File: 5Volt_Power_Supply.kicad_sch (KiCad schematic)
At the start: 12 parts, among them J1 Screw_Terminal_01x02, J2 Screw_Terminal_01x02, U1 L7805

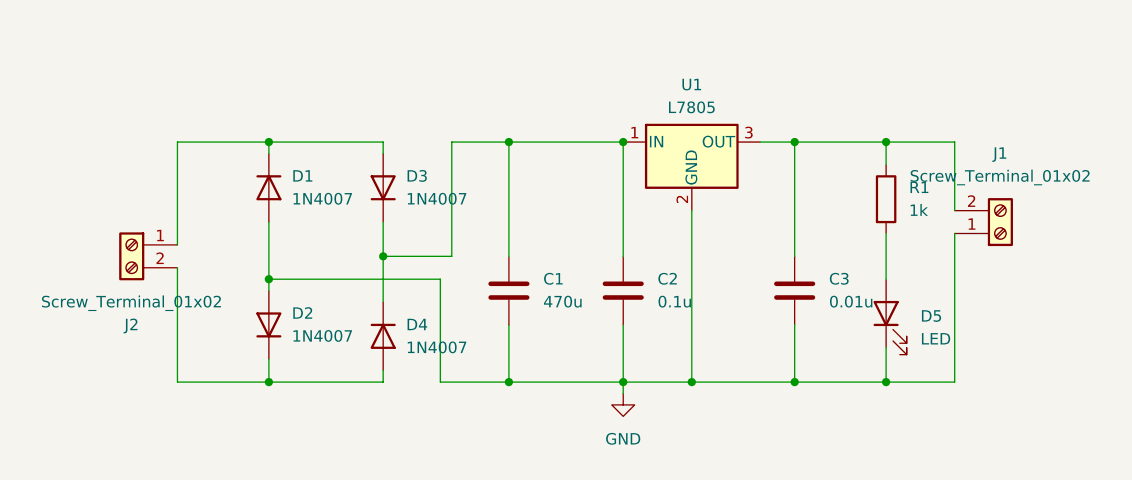
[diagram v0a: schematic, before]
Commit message: schematic pcb views
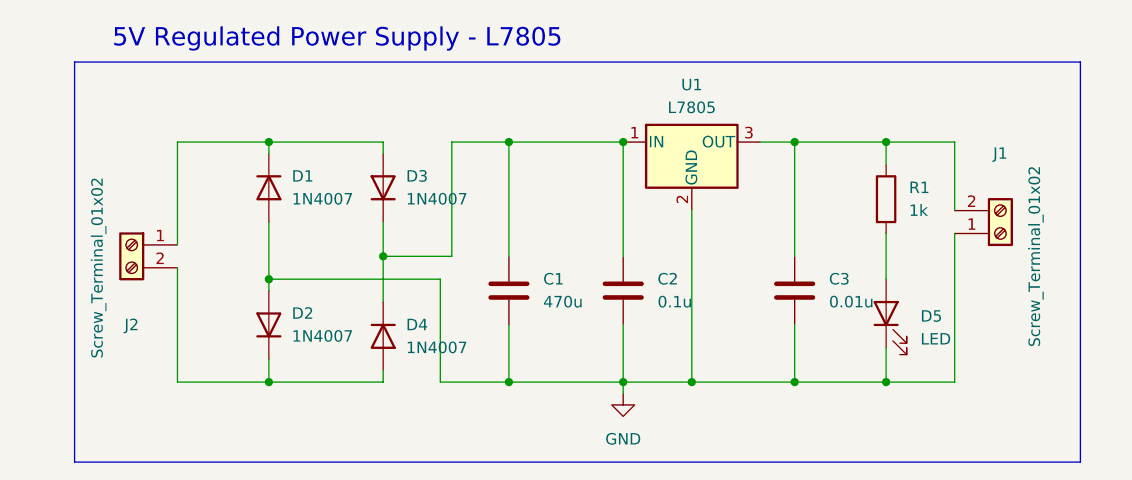
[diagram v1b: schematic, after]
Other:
- note added: "5V Regulated Power Supply - L7805"
- company: IBrahim Jarallah -> Ibrahim Jarallah
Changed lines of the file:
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@@
 		(date "2026-02-27")
 		(rev "1.0")
-		(company "IBrahim Jarallah")
+		(company "Ibrahim Jarallah")
+	)
+	(rectangle
+		(start 100.33 30.48)
+		(end 212.09 74.93)
+		(stroke
+			(width 0.0254)
+			(type solid)
+			(color 0 0 0 1)
+		)
+		(fill
+			(type none)
+		)
+	)
+	(text "5V Regulated Power Supply - L7805"
+		(exclude_from_sim no)
+		(at 129.54 27.94 0)
+		(effects
+			(font
+				(size 2.032 2.032)
+				(thickness 0.254)
+				(color 0 0 0 1)
+			)
+		)
 	)
 	(junction
@@
 		)
 		(property "Value" "Screw_Terminal_01x02"
-			(at 106.68 57.15 0)
+			(at 102.87 53.34 90)
 			(effects
 				(font
@@
 		)
 		(property "Value" "Screw_Terminal_01x02"
-			(at 203.2 43.18 0)
-			(effects
-				(font
+			(at 207.01 52.07 90)
+			(effects
+				(font
